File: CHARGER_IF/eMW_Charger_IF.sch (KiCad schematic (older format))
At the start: 15 parts, among them J1 CONN_01X02, J2 Booster_J1_J3, J3 Booster_J4_J2, J4 CONN_02X10, J5 CONN_02X10, U1 V7805-2000R, U2 Arduino-Socket, U3 SN74ACT08N, U4 SN74ACT08N

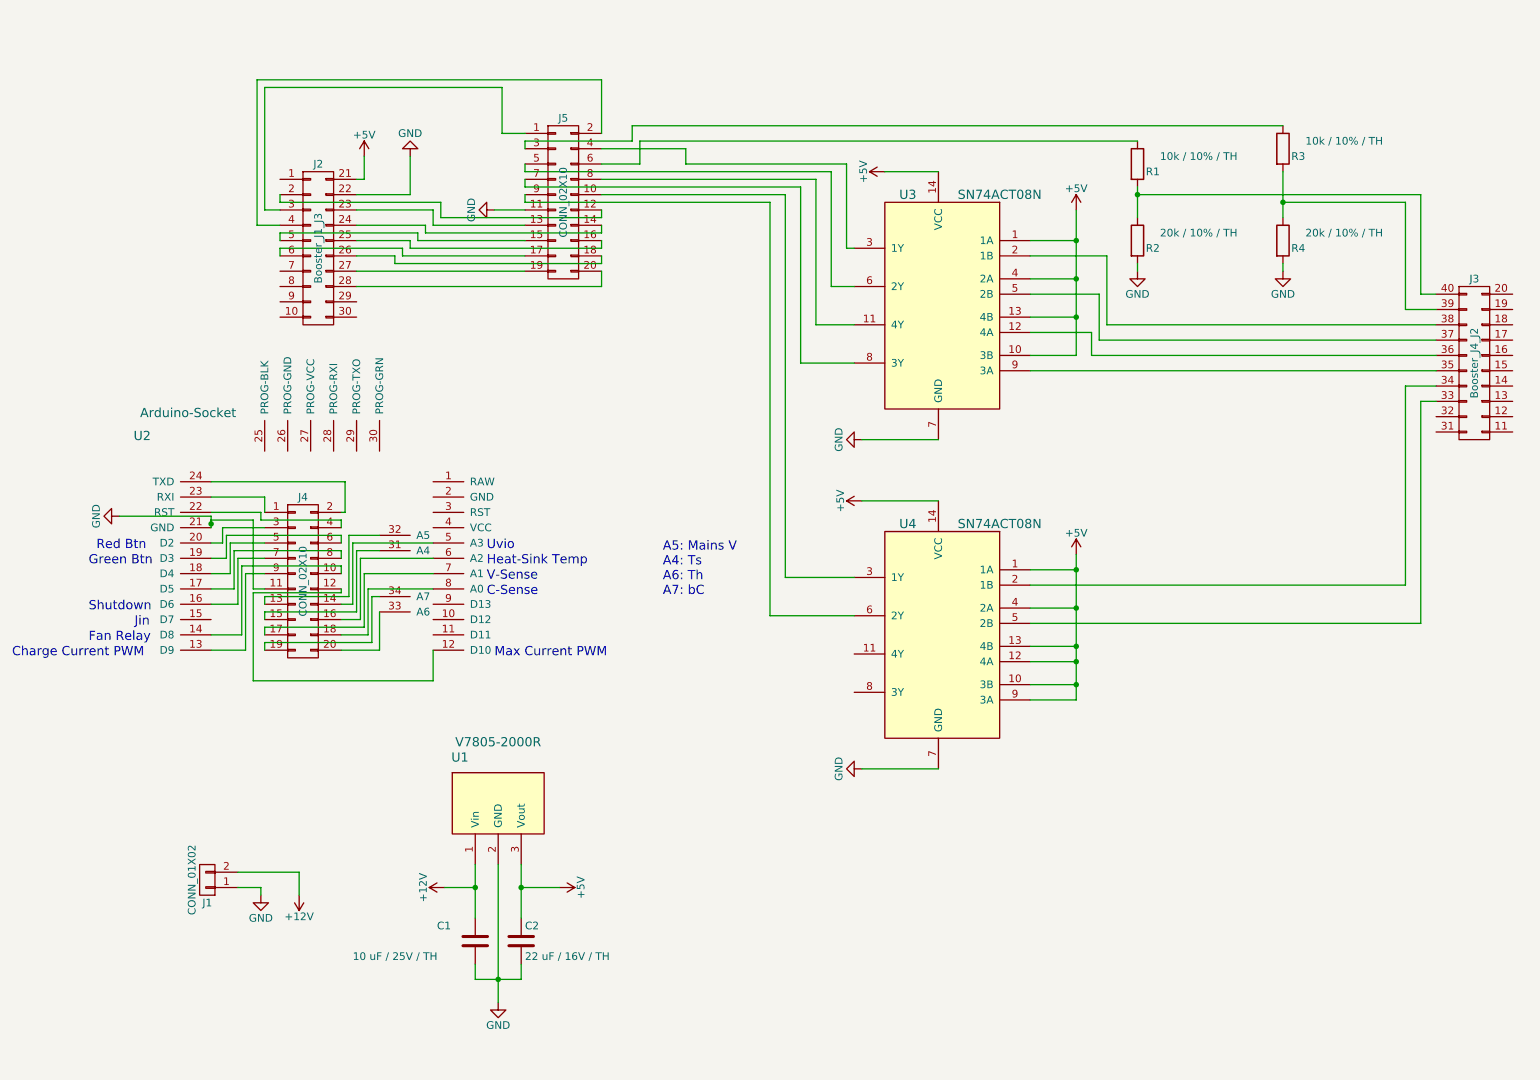
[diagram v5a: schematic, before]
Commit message: Charger IF WIP
Mostly just need to double check all the mechanics and add a few
mounting holes
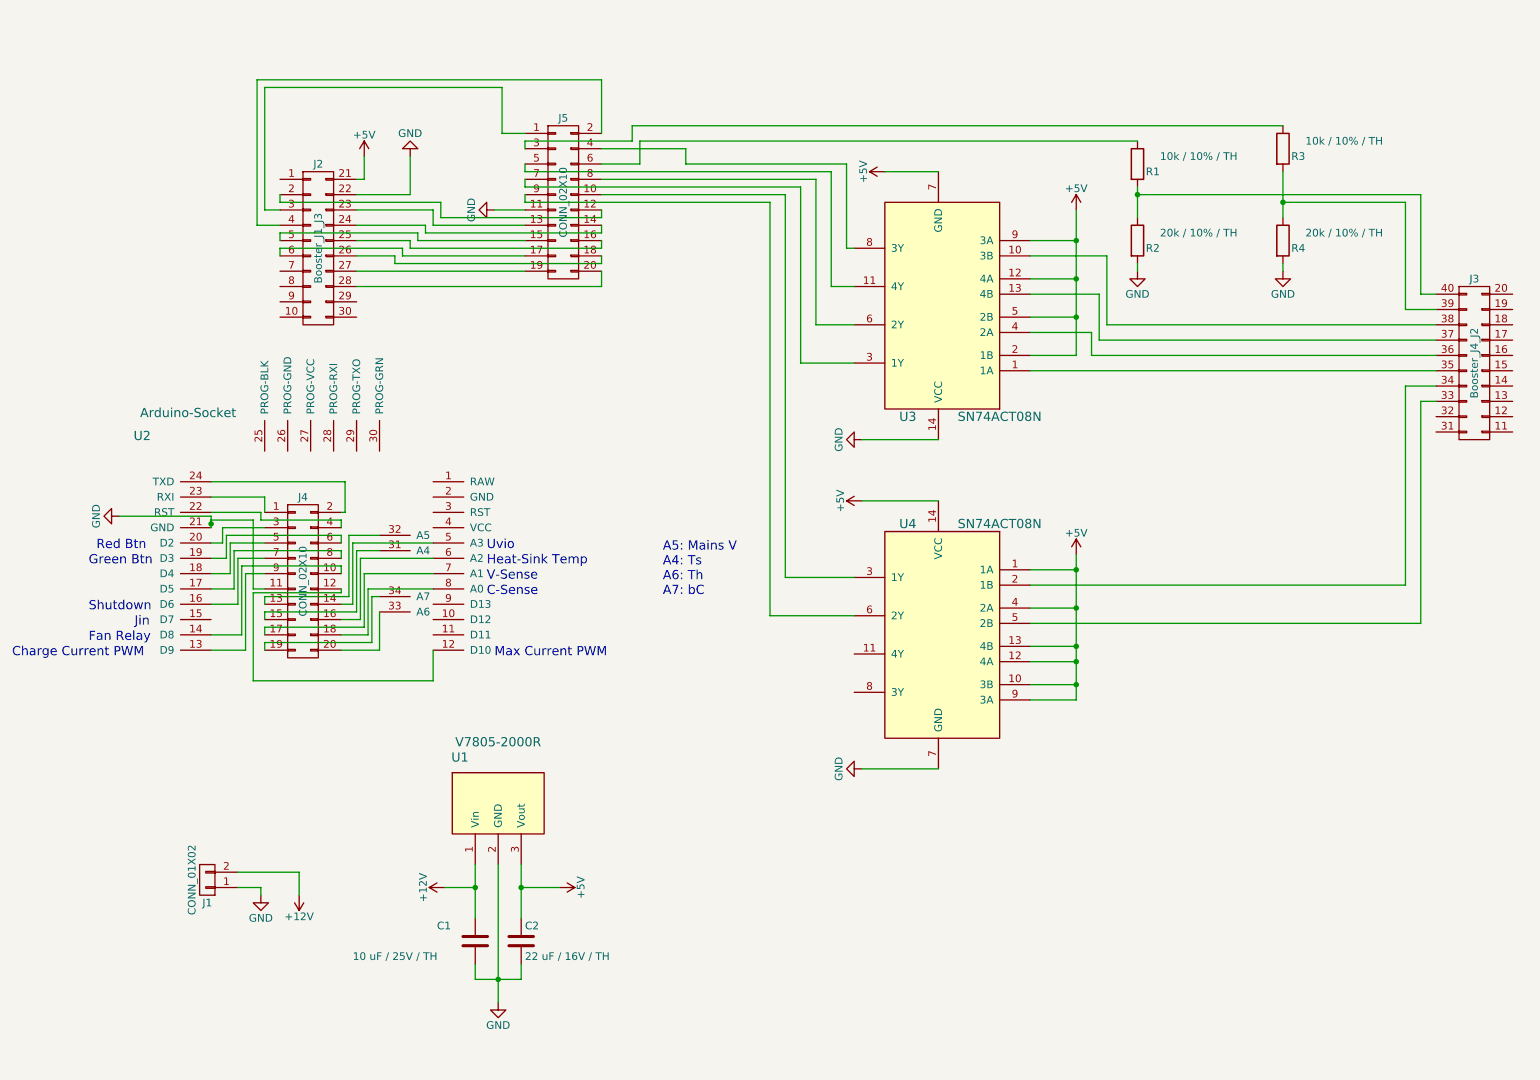
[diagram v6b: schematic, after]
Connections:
- net +5V: now also U3.12 (4A), U3.2 (1B), U3.5 (2B), U3.7 (GND), U3.9 (3A); no longer U3.1 (1A), U3.10 (3B), U3.13 (4B), U3.14 (VCC), U3.4 (2A)
- net GND: now also U3.14 (VCC); no longer U3.7 (GND)
- net at U3.11 (4Y): now also J5.5 (P5); no longer J5.8 (P8)
- net at J3.36 (P36): now also U3.4 (2A); no longer U3.12 (4A)
- net at J3.38 (P38): now also U3.10 (3B); no longer U3.2 (1B)
- net at U3.3 (1Y): now also J5.7 (P7); no longer J5.4 (P4)
- net at J3.37 (P37): now also U3.13 (4B); no longer U3.5 (2B)
- net at U3.6 (2Y): now also J5.8 (P8); no longer J5.5 (P5)
- net at U3.8 (3Y): now also J5.4 (P4); no longer J5.7 (P7)
- net at J3.35 (P35): now also U3.1 (1A); no longer U3.9 (3A)
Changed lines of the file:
@@
 L SN74LS08N U3
 U 1 1 59742C3C
-P 6850 2450
-F 0 "U3" H 7050 3150 60  0000 C CNN
-F 1 "SN74ACT08N" H 6450 3150 60  0000 C CNN
-F 2 "Housings_DIP:DIP-14_W7.62mm" H 6850 2450 60  0001 C CNN
-F 3 "" H 6850 2450 60  0000 C CNN
-F 4 "595-SN74ACT08N" H 6850 2450 60  0001 C CNN "Mouser PN"
-F 5 "http://www.mouser.com/search/ProductDetail.aspx?R=0virtualkey0virtualkeySN74ACT08N" H 6850 2450 60  0001 C CNN "Mouser URL"
-	1    6850 2450
-	-1   0    0    -1
+P 6850 2500
+F 0 "U3" H 7050 3200 60  0000 C CNN
+F 1 "SN74ACT08N" H 6450 3200 60  0000 C CNN
+F 2 "Housings_DIP:DIP-14_W7.62mm" H 6850 2500 60  0001 C CNN
+F 3 "" H 6850 2500 60  0000 C CNN
+F 4 "595-SN74ACT08N" H 6850 2500 60  0001 C CNN "Mouser PN"
+F 5 "http://www.mouser.com/search/ProductDetail.aspx?R=0virtualkey0virtualkeySN74ACT08N" H 6850 2500 60  0001 C CNN "Mouser URL"
+	1    6850 2500
+	-1   0    0    1
 $EndComp
 $Comp
@@
 	3625 6275 3825 6275
 Wire Wire Line
-	3825 6125 3825 6475
-Wire Wire Line
-	3975 6125 3975 7025
+	3825 6125 3825 6275
+Wire Wire Line
+	3825 6275 3825 6475
+Wire Wire Line
+	3975 6125 3975 6875
+Wire Wire Line
+	3975 6875 3975 7025
 Wire Wire Line
 	6500 1600 6850 1600
@@
 	6850 5500 6350 5500
 Wire Wire Line
-	7750 4100 7750 5050
+	7750 4100 7750 4200
+Wire Wire Line
+	7750 4200 7750 4450
+Wire Wire Line
+	7750 4450 7750 4700
+Wire Wire Line
+	7750 4700 7750 4800
+Wire Wire Line
+	7750 4800 7750 4950
+Wire Wire Line
+	7750 4950 7750 5050
 Wire Wire Line
 	7750 4200 7450 4200
@@
 	7450 2050 7750 2050
 Wire Wire Line
-	7750 1850 7750 2800
+	7750 1850 7750 2050
+Wire Wire Line
+	7750 2050 7750 2300
+Wire Wire Line
+	7750 2300 7750 2550
+Wire Wire Line
+	7750 2550 7750 2800
 Wire Wire Line
 	7750 2300 7450 2300
@@
 Connection ~ 7750 2550
 Wire Wire Line
-	8150 1700 8150 1900
-Wire Wire Line
-	9100 1600 9100 1900
+	8150 1700 8150 1750
+Wire Wire Line
+	8150 1750 8150 1900
+Wire Wire Line
+	9100 1600 9100 1800
+Wire Wire Line
+	9100 1800 9100 1900
 Wire Wire Line
 	8150 2250 8150 2200
@@
 	2550 1950 2400 1950
 Wire Wire Line
-	4125 6125 4125 6475
+	4125 6125 4125 6275
+Wire Wire Line
+	4125 6275 4125 6475
 Wire Wire Line
 	4125 6275 4375 6275
@@
 	4125 6875 4125 6775
 Wire Wire Line
-	3825 6875 4125 6875
+	3825 6875 3975 6875
+Wire Wire Line
+	3975 6875 4125 6875
 Connection ~ 3975 6875
 Wire Wire Line
@@
 	2375 3875 2100 3875
 Wire Wire Line
-	2100 3875 2100 3925
+	2100 3875 2100 3900
+Wire Wire Line
+	2100 3900 2100 3925
 Wire Wire Line
 	4150 1350 4000 1350

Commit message: updated to osh park design rules
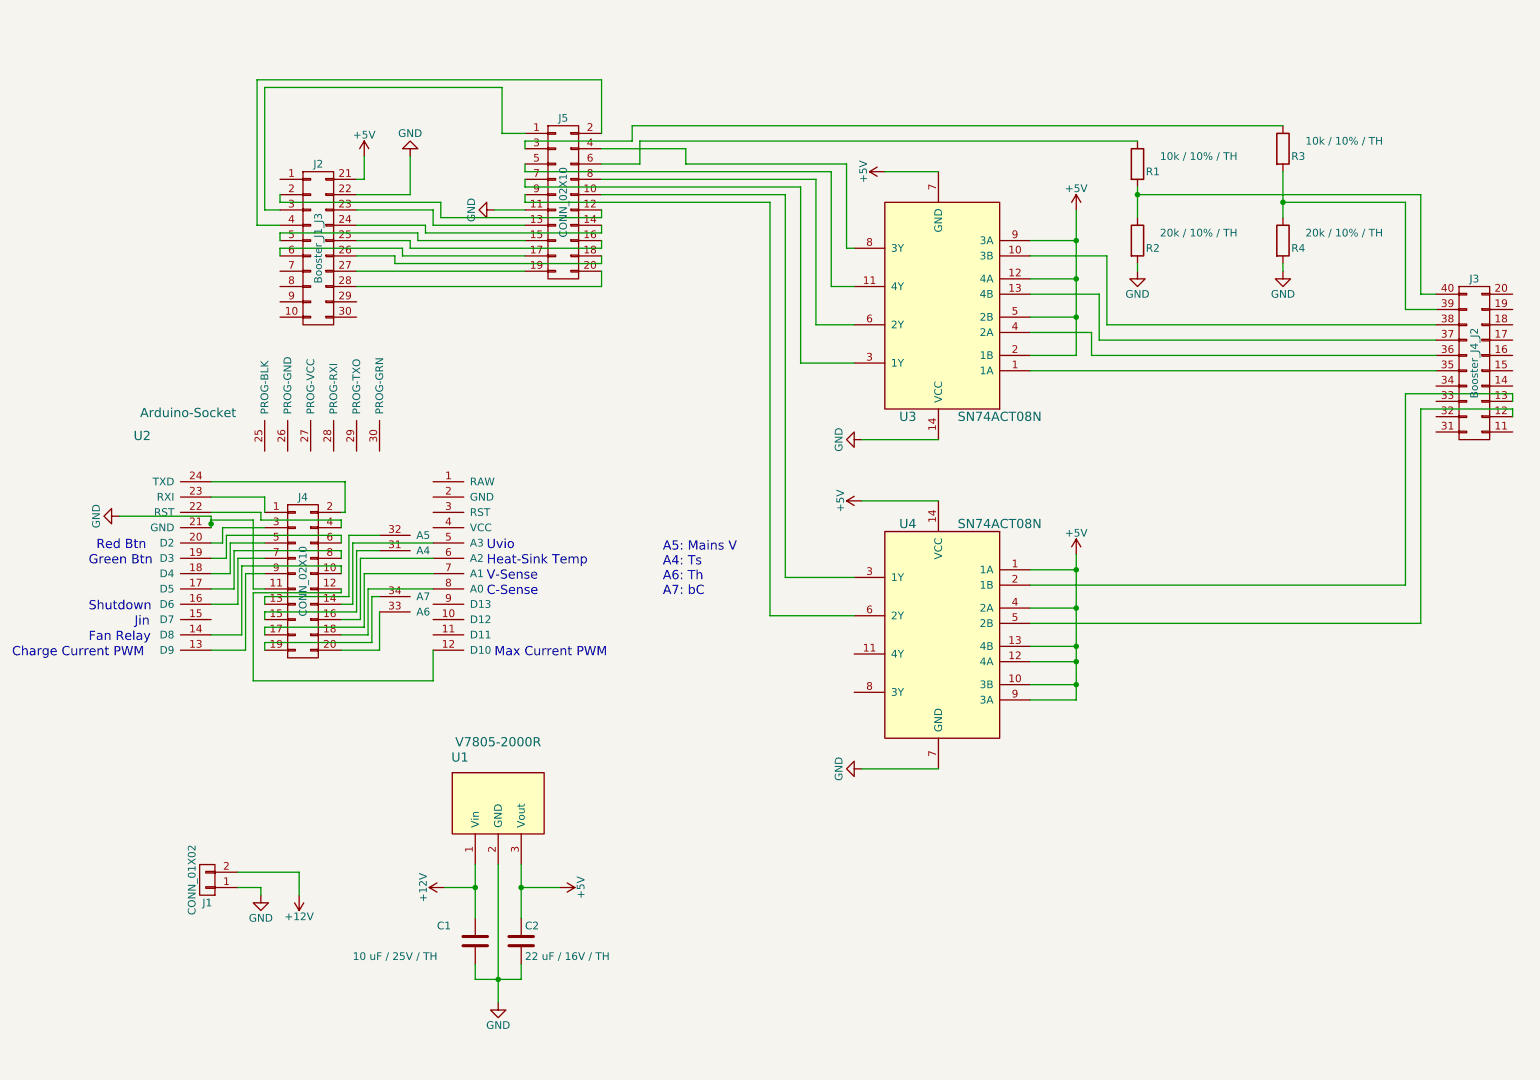
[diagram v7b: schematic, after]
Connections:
- net at U4.2 (1B): now also J3.13 (P13); no longer J3.34 (P34)
- net at U4.5 (2B): now also J3.12 (P12); no longer J3.33 (P33)

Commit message: Charger IF
Just need to do a once over before ordering
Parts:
- C1, C2: footprint Capacitors_THT:CP_Radial_D6.3mm_P2.50mm -> Capacitors_THT:C_Disc_D8.0mm_W5.0mm_P5.00mm
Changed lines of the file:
@@
 F 0 "C1" H 3575 6725 50  0000 L CNN
 F 1 "10 uF / 25V / TH" H 3025 6525 50  0000 L CNN
-F 2 "Capacitors_THT:CP_Radial_D6.3mm_P2.50mm" H 3863 6475 50  0001 C CNN
+F 2 "Capacitors_THT:C_Disc_D8.0mm_W5.0mm_P5.00mm" H 3863 6475 50  0001 C CNN
 F 3 "" H 3825 6625 50  0000 C CNN
 F 4 "810-FG26X7R1E106KRT6" H 3825 6625 60  0001 C CNN "Mouser PN"
@@
 F 0 "C2" H 4150 6725 50  0000 L CNN
 F 1 "22 uF / 16V / TH" H 4150 6525 50  0000 L CNN
-F 2 "Capacitors_THT:CP_Radial_D6.3mm_P2.50mm" H 4163 6475 50  0001 C CNN
+F 2 "Capacitors_THT:C_Disc_D8.0mm_W5.0mm_P5.00mm" H 4163 6475 50  0001 C CNN
 F 3 "" H 4125 6625 50  0000 C CNN
 F 4 "810-FG22X7R1E226MRT6" H 4125 6625 60  0001 C CNN "Mouser PN"
